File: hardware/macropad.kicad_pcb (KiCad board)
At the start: 2 copper layers, 63.5 x 106.7 mm, 28 parts, among them J1 Conn_01x02, J2 Conn_01x06, J3 I2C Screen, J4 SPI Screen, SW1 SW_Push, SW10 SW_Push, SW2 SW_Push, SW3 SW_Push, SW4 SW_Push, SW5 SW_Push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

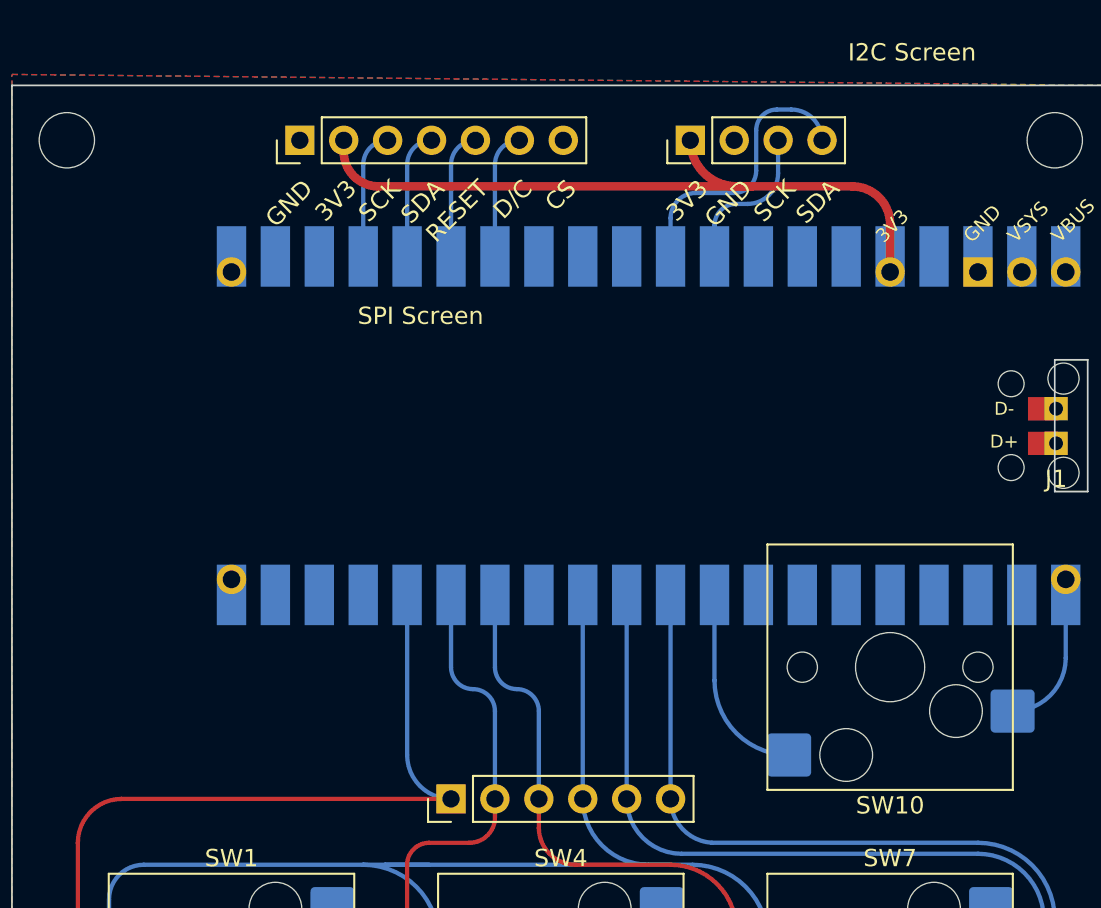
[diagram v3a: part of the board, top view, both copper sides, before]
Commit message: :truck: Move screen headers, before changing footprint
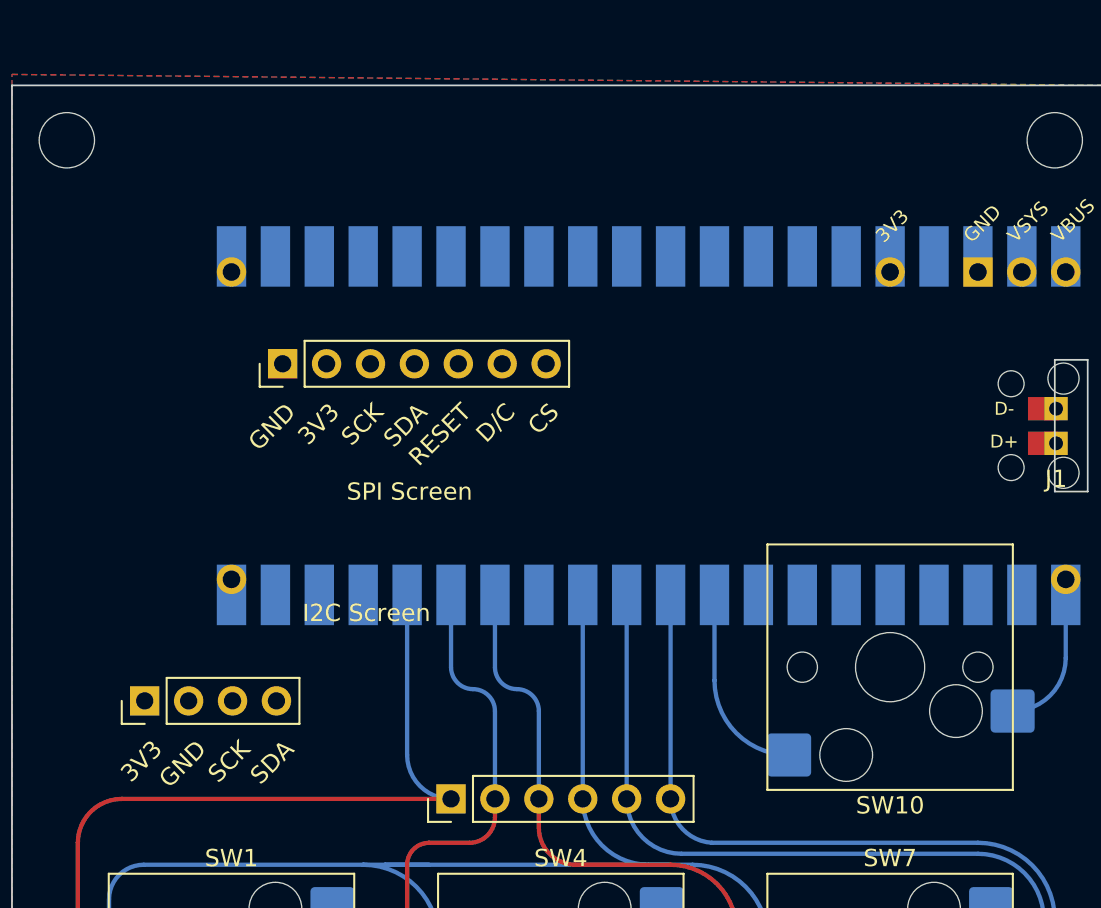
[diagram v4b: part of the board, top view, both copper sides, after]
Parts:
- moved J3 45.3 mm to (71.2, 59.1)
- moved J4 13.0 mm to (79.2, 39.6)
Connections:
- U1 pad 19: unconnected-(U1-Pad19) -> SDA
- U1 pad 20: unconnected-(U1-Pad20) -> SCK
- U1 pad 31: SDA -> unconnected-(U1-Pad31)
- U1 pad 32: SCK -> unconnected-(U1-Pad32)
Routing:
- net 3V3: track 42.2 -> 0.00 mm
- net SDA: track 17.3 -> 0.00 mm
- net SCK: track 9.89 -> 0.00 mm
- net SPI0_SCK: track 8.37 -> 0.00 mm
- net SCREEN_COMMAND: track 8.37 -> 0.00 mm
- net SCREEN_RESET: track 8.37 -> 0.00 mm
- net SPI0_TX: track 8.37 -> 0.00 mm
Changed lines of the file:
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@@
   (net 26 "unconnected-(U1-Pad17)")
   (net 27 "SPI0_SCK")
-  (net 28 "unconnected-(U1-Pad19)")
-  (net 29 "unconnected-(U1-Pad20)")
+  (net 28 "unconnected-(U1-Pad31)")
+  (net 29 "unconnected-(U1-Pad32)")
   (net 30 "SPI0_TX")
   (net 31 "SCREEN_RESET")
@@
   )
   (footprint "Connector_PinHeader_2.54mm:PinHeader_1x07_P2.54mm_Vertical" (layer "F.Cu")
-    (at 80.1525 26.67 90)
+    (at 79.16 39.6 90)
     (descr "Through hole straight pin header, 1x07, 2.54mm pitch, single row")
     (tags "Through hole pin header THT 1x07 2.54mm single row")
@@
       (effects (font (size 1 1) (thickness 0.15)))
     )
-    (fp_text value "SPI Screen" (at -10.16 6.985) (layer "F.SilkS")
+    (fp_text value "SPI Screen" (at -7.4 7.34) (layer "F.SilkS")
       (effects (font (size 1 1) (thickness 0.15)))
     )
@@
     (pad "6" thru_hole oval (at 0 12.7 90) (size 1.7 1.7) (drill 1) (layers *.Cu *.Mask)
       (net 5 "ROW3") (pinfunction "Pin_6") (pintype "passive"))
-    (model "${KICAD6_3DMODEL_DIR}/Connector_PinHeader_2.54mm.3dshapes/PinHeader_1x06_P2.54mm_Vertical.wrl"
-      (offset (xyz 0 0 0))
-      (scale (xyz 1 1 1))
-      (rotate (xyz 0 0 0))
-    )
   )
   (footprint "Switch_Keyboard_Hotswap_Kailh:SW_Hotswap_Kailh_MX" (layer "F.Cu")
@@
   )
   (footprint "Connector_PinHeader_2.54mm:PinHeader_1x04_P2.54mm_Vertical" (layer "F.Cu")
-    (at 102.74103 26.67 90)
+    (at 71.18 59.1 90)
     (descr "Through hole straight pin header, 1x04, 2.54mm pitch, single row")
     (tags "Through hole pin header THT 1x04 2.54mm single row")
@@
       (net 16 "GND") (pinfunction "GND") (pintype "power_in"))
     (pad "19" smd rect (at -8.89 -21.59 90) (size 3.5 1.7) (drill (offset -0.9 0)) (layers "B.Cu" "B.Mask")
-      (net 28 "unconnected-(U1-Pad19)") (pinfunction "GPIO14") (pintype "bidirectional"))
+      (net 18 "SDA") (pinfunction "GPIO14") (pintype "bidirectional"))
     (pad "20" smd rect (at -8.89 -24.13 90) (size 3.5 1.7) (drill (offset -0.9 0)) (layers "B.Cu" "B.Mask")
-      (net 29 "unconnected-(U1-Pad20)") (pinfunction "GPIO15") (pintype "bidirectional"))
+      (net 17 "SCK") (pinfunction "GPIO15") (pintype "bidirectional"))
     (pad "20" thru_hole oval (at -8.89 -24.13 90) (size 1.7 1.7) (drill 1.02) (layers *.Cu *.Mask)
-      (net 29 "unconnected-(U1-Pad20)") (pinfunction "GPIO15") (pintype "bidirectional"))
+      (net 17 "SCK") (pinfunction "GPIO15") (pintype "bidirectional"))
     (pad "21" smd rect (at 8.89 -24.13 90) (size 3.5 1.7) (drill (offset 0.9 0)) (layers "B.Cu" "B.Mask")
       (net 25 "unconnected-(U1-Pad21)") (pinfunction "GPIO16") (pintype "bidirectional"))
@@
       (net 35 "unconnected-(U1-Pad30)") (pinfunction "RUN") (pintype "input"))
     (pad "31" smd rect (at 8.89 1.27 90) (size 3.5 1.7) (drill (offset 0.9 0)) (layers "B.Cu" "B.Mask")
-      (net 18 "SDA") (pinfunction "GPIO26_ADC0") (pintype "bidirectional"))
+      (net 28 "unconnected-(U1-Pad31)") (pinfunction "GPIO26_ADC0") (pintype "bidirectional"))
     (pad "32" smd rect (at 8.89 3.81 90) (size 3.5 1.7) (drill (offset 0.9 0)) (layers "B.Cu" "B.Mask")
-      (net 17 "SCK") (pinfunction "GPIO27_ADC1") (pintype "bidirectional"))
+      (net 29 "unconnected-(U1-Pad32)") (pinfunction "GPIO27_ADC1") (pintype "bidirectional"))
     (pad "33" smd rect (at 8.89 6.35 90) (size 3.5 1.7) (drill (offset 0.9 0)) (layers "B.Cu" "B.Mask")
       (net 16 "GND") (pinfunction "AGND") (pintype "power_in"))
@@
   (gr_line (start 63.5 130.175) (end 127 130.175) (layer "Edge.Cuts") (width 0.1))
   (gr_line (start 63.5 23.495) (end 63.5 130.175) (layer "Edge.Cuts") (width 0.1))
-  (gr_text "SDA" (at 88.265 29.21 45) (layer "F.SilkS")
+  (gr_text "SDA" (at 87.2725 42.14 45) (layer "F.SilkS")
     (effects (font (size 1 1) (thickness 0.15)) (justify right))
   )
-  (gr_text "RESET" (at 90.805 29.21 45) (layer "F.SilkS")
+  (gr_text "RESET" (at 89.8125 42.14 45) (layer "F.SilkS")
     (effects (font (size 1 1) (thickness 0.15)) (justify right))
   )
-  (gr_text "GND" (at 106.045 29.21 45) (layer "F.SilkS")
+  (gr_text "GND" (at 74.48397 61.64 45) (layer "F.SilkS")
     (effects (font (size 1 1) (thickness 0.15)) (justify right))
   )
-  (gr_text "D/C" (at 93.345 29.21 45) (layer "F.SilkS")
+  (gr_text "D/C" (at 92.3525 42.14 45) (layer "F.SilkS")
     (effects (font (size 1 1) (thickness 0.15)) (justify right))
   )
-  (gr_text "SCK\n" (at 85.725 29.21 45) (layer "F.SilkS")
+  (gr_text "SCK\n" (at 84.7325 42.14 45) (layer "F.SilkS")
     (effects (font (size 1 1) (thickness 0.15)) (justify right))
   )
-  (gr_text "SDA" (at 111.125 29.21 45) (layer "F.SilkS")
+  (gr_text "SDA" (at 79.56397 61.64 45) (layer "F.SilkS")
     (effects (font (size 1 1) (thickness 0.15)) (justify right))
   )
-  (gr_text "GND" (at 80.645 29.21 45) (layer "F.SilkS")
+  (gr_text "GND" (at 79.6525 42.14 45) (layer "F.SilkS")
     (effects (font (size 1 1) (thickness 0.15)) (justify right))
   )
@@
     (effects (font (size 0.8 0.8) (thickness 0.15)) (justify left))
   )
-  (gr_text "CS" (at 95.885 29.21 45) (layer "F.SilkS")
+  (gr_text "CS" (at 94.8925 42.14 45) (layer "F.SilkS")
     (effects (font (size 1 1) (thickness 0.15)) (justify right))
   )
@@
     (effects (font (size 0.75 0.75) (thickness 0.15)))
   )
-  (gr_text "3V3" (at 83.185 29.21 45) (layer "F.SilkS")
+  (gr_text "3V3" (at 82.1925 42.14 45) (layer "F.SilkS")
     (effects (font (size 1 1) (thickness 0.15)) (justify right))
   )
-  (gr_text "SCK\n" (at 108.585 29.21 45) (layer "F.SilkS")
+  (gr_text "SCK\n" (at 77.02397 61.64 45) (layer "F.SilkS")
     (effects (font (size 1 1) (thickness 0.15)) (justify right))
   )
-  (gr_text "3V3" (at 103.505 29.21 45) (layer "F.SilkS")
+  (gr_text "3V3" (at 71.94397 61.64 45) (layer "F.SilkS")
     (effects (font (size 1 1) (thickness 0.15)) (justify right))
   )
@@
   (arc (start 92.71 58.42) (mid 93.608026 58.791974) (end 93.98 59.69) (width 0.25) (layer "B.Cu") (net 15))
   (arc (start 91.44 57.15) (mid 91.811974 58.048026) (end 92.71 58.42) (width 0.25) (layer "B.Cu") (net 15))
-  (segment (start 106.045 30.353) (end 105.380608 30.353) (width 0.25) (layer "B.Cu") (net 17))
-  (segment (start 104.14 34.29) (end 104.14 31.593608) (width 0.25) (layer "B.Cu") (net 17))
-  (segment (start 107.82103 28.57697) (end 107.82103 26.67) (width 0.25) (layer "B.Cu") (net 17))
-  (arc (start 106.045 30.353) (mid 107.300843 29.832813) (end 107.82103 28.57697) (width 0.25) (layer "B.Cu") (net 17))
-  (arc (start 104.14 31.593608) (mid 104.503366 30.716366) (end 105.380608 30.353) (width 0.25) (layer "B.Cu") (net 17))
-  (segment (start 108.58303 24.892) (end 107.747042 24.892) (width 0.25) (layer "B.Cu") (net 18))
-  (segment (start 106.553 26.086042) (end 106.553 28.432663) (width 0.25) (layer "B.Cu") (net 18))
-  (segment (start 105.267663 29.718) (end 103.053719 29.718) (width 0.25) (layer "B.Cu") (net 18))
-  (segment (start 101.6 31.171719) (end 101.6 34.29) (width 0.25) (layer "B.Cu") (net 18))
-  (arc (start 110.36103 26.67) (mid 109.840266 25.412764) (end 108.58303 24.892) (width 0.25) (layer "B.Cu") (net 18))
-  (arc (start 107.747042 24.892) (mid 106.902727 25.241727) (end 106.553 26.086042) (width 0.25) (layer "B.Cu") (net 18))
-  (arc (start 106.553 28.432663) (mid 106.176534 29.341534) (end 105.267663 29.718) (width 0.25) (layer "B.Cu") (net 18))
-  (arc (start 103.053719 29.718) (mid 102.025784 30.143784) (end 101.6 31.171719) (width 0.25) (layer "B.Cu") (net 18))
-  (segment (start 106.299 29.337) (end 112.116231 29.337) (width 0.5) (layer "F.Cu") (net 20))
-  (segment (start 106.299 29.337) (end 105.40803 29.337) (width 0.5) (layer "F.Cu") (net 20))
-  (segment (start 114.3 34.29) (end 114.3 31.520769) (width 0.5) (layer "F.Cu") (net 20))
-  (segment (start 84.691049 29.337) (end 106.299 29.337) (width 0.5) (layer "F.Cu") (net 20))
-  (segment (start 82.6925 26.67) (end 82.6925 27.338451) (width 0.5) (layer "F.Cu") (net 20))
-  (arc (start 112.116231 29.337) (mid 113.660389 29.976611) (end 114.3 31.520769) (width 0.5) (layer "F.Cu") (net 20))
-  (arc (start 82.6925 27.338451) (mid 83.277861 28.751639) (end 84.691049 29.337) (width 0.5) (layer "F.Cu") (net 20))
-  (arc (start 105.40803 29.337) (mid 103.522176 28.555854) (end 102.74103 26.67) (width 0.5) (layer "F.Cu") (net 20))
-  (segment (start 83.82 28.0825) (end 83.82 34.29) (width 0.25) (layer "B.Cu") (net 27))
-  (arc (start 85.2325 26.67) (mid 84.233712 27.083712) (end 83.82 28.0825) (width 0.25) (layer "B.Cu") (net 27))
-  (segment (start 86.36 28.0825) (end 86.36 34.29) (width 0.25) (layer "B.Cu") (net 30))
-  (arc (start 87.7725 26.67) (mid 86.773712 27.083712) (end 86.36 28.0825) (width 0.25) (layer "B.Cu") (net 30))
-  (segment (start 88.9 28.0825) (end 88.9 34.29) (width 0.25) (layer "B.Cu") (net 31))
-  (arc (start 90.3125 26.67) (mid 89.313712 27.083712) (end 88.9 28.0825) (width 0.25) (layer "B.Cu") (net 31))
-  (segment (start 91.44 28.0825) (end 91.44 34.29) (width 0.25) (layer "B.Cu") (net 32))
-  (arc (start 92.8525 26.67) (mid 91.853712 27.083712) (end 91.44 28.0825) (width 0.25) (layer "B.Cu") (net 32))
   (segment (start 124.46 56.615) (end 124.46 52.07) (width 0.25) (layer "B.Cu") (net 41))
   (arc (start 121.385 59.69) (mid 123.559353 58.789353) (end 124.46 56.615) (width 0.25) (layer "B.Cu") (net 41))

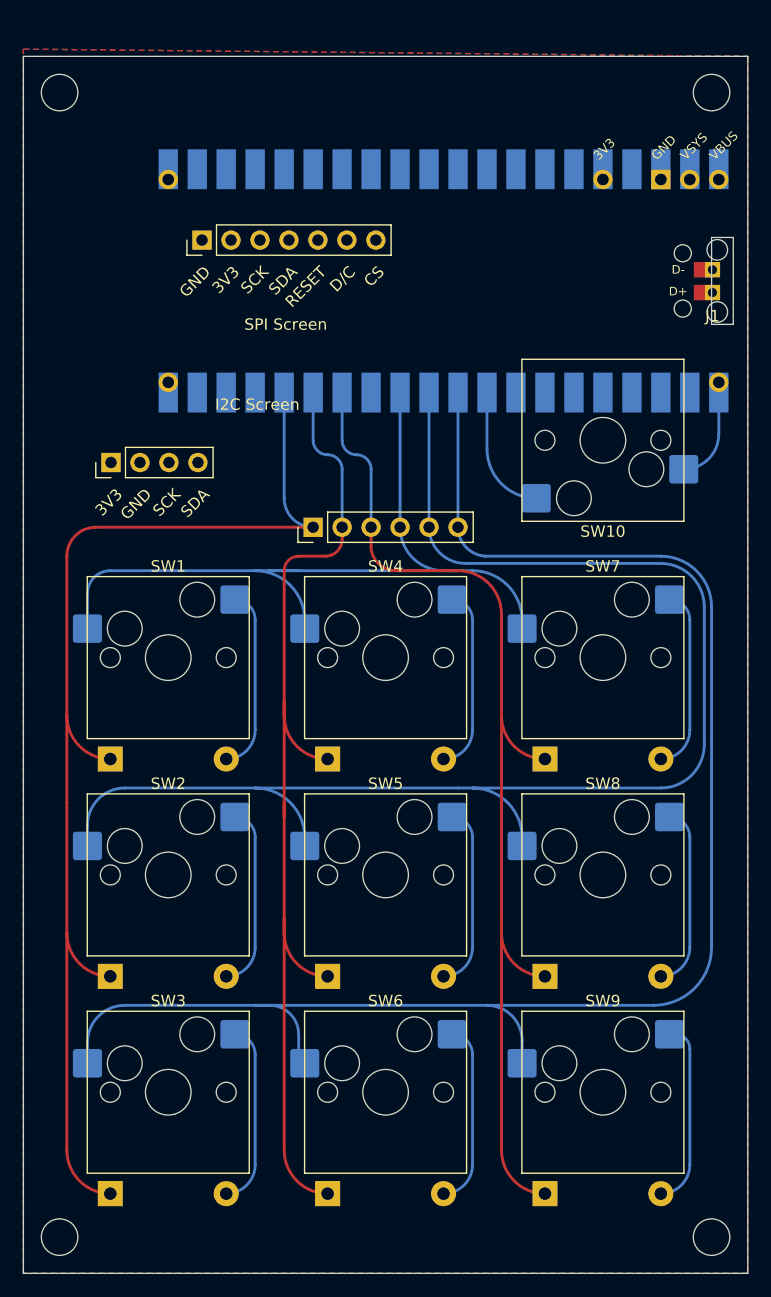
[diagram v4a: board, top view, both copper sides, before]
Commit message: :construction: Change OLED footprint, reroute to accomodate. Delete USB pads, leave hole instead
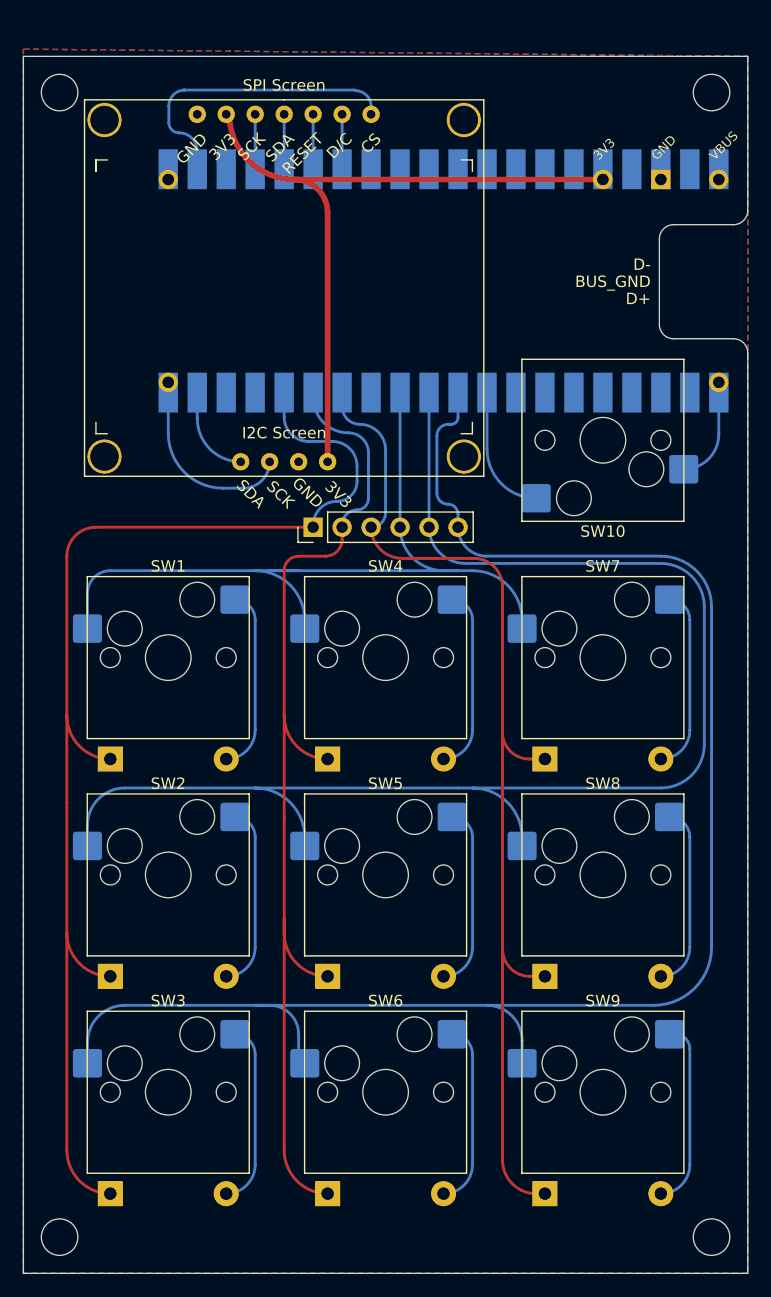
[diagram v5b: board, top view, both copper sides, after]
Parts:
- removed J1: Conn_01x02, Connector_PinHeader_2.00mm:PinHeader_1x02_P2.00mm_Vertical
- J3: footprint Connector_PinHeader_2.54mm:PinHeader_1x04_P2.54mm_Vertical -> nn_lib:I2C_1.3inch_OLED
- J4: footprint Connector_PinHeader_2.54mm:PinHeader_1x07_P2.54mm_Vertical -> nn_lib:SPI_1.3inch_OLED
- moved J3 15.2 mm to (86.4, 59.0), turned to 180 degrees
- moved J4 13.2 mm to (86.4, 28.6), turned to 0 degrees
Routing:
- net 3V3: track 0.00 -> 62.3 mm
- net SPI0_CS: track 0.00 -> 27.7 mm
- net SCK: track 0.00 -> 17.1 mm
- net SDA: track 0.00 -> 8.99 mm
- net SPI0_TX: track 0.00 -> 5.71 mm
- net SPI0_SCK: track 0.00 -> 5.71 mm
- net SCREEN_RESET: track 0.00 -> 5.71 mm
- net SCREEN_COMMAND: track 0.00 -> 5.71 mm
- net COL1: track 106.6 -> 111.6 mm
- net ROW3: track 144.1 -> 146.2 mm
- net COL3: track 96.1 -> 95.2 mm
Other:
- outline, holes or cut-outs redrawn
- board text added: "<- USB THIS WAY"
- board text added: "BUS_GND"
- board text removed: "VSYS"
